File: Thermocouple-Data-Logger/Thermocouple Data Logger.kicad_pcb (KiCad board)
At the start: 4 copper layers, 75 x 85 mm, 149 parts, among them J0 Power, J1 Micro_SD_Card_Det, J2 Probe 1, J3 Probe 2, J4 Probe 3, J5 Probe 4, J6 ISP, SW0 Power, SW1 Display, SW2 Reset, SW3 Select/Calibrate, SW4 Cycle/Menu, SW5 SW_DIP_x04, U0 ATMEGA324PA-MU, U1 LT1763-3.3, U10 74HC595, U11 HDSP-521E-Display, U12 HDSP-521E-Display, U13 4050, U2 MAX31856, U3 MAX31856, U4 MAX31856, U5 MAX31856, U6 74HC595, U7 74HC595, U8 74HC595, U9 74HC595, Y0 10MHz, Y1 32.768KHz

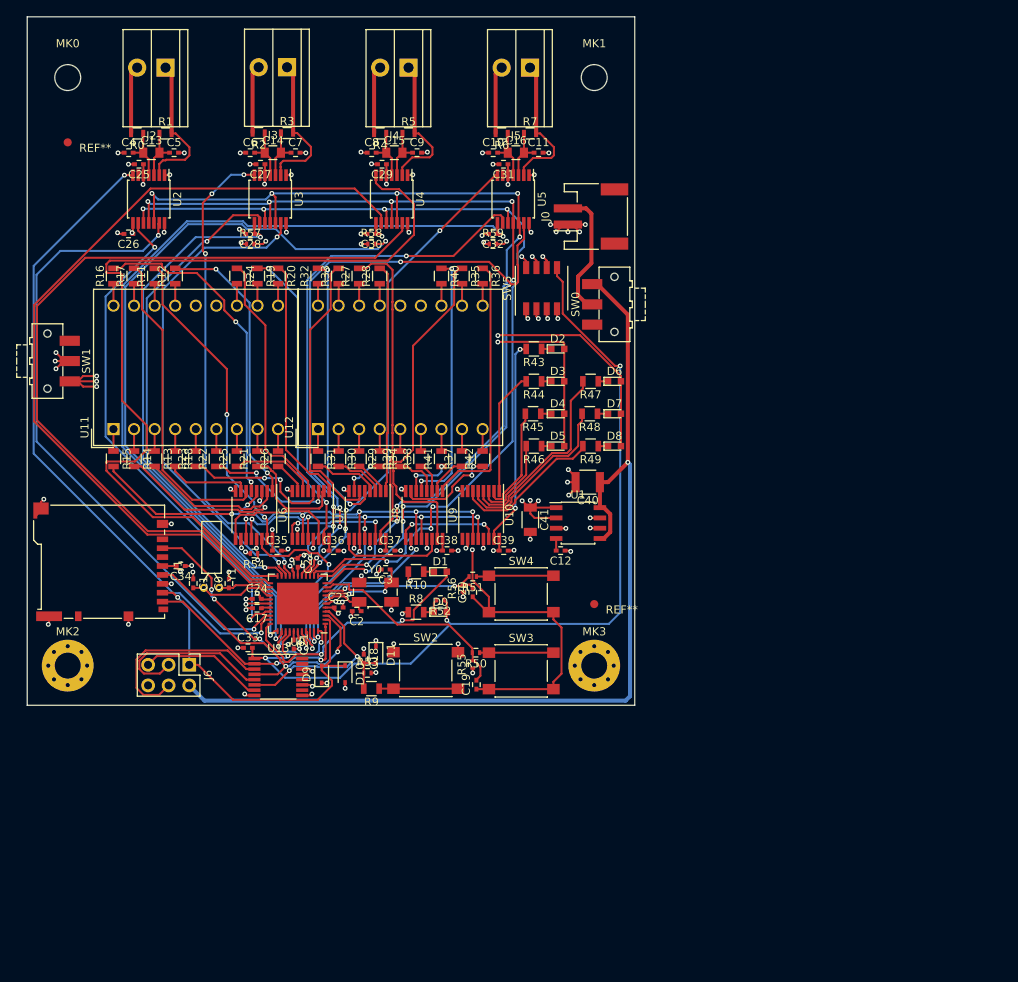
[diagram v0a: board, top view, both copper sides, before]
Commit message: Centerd board and generated gerber for test view
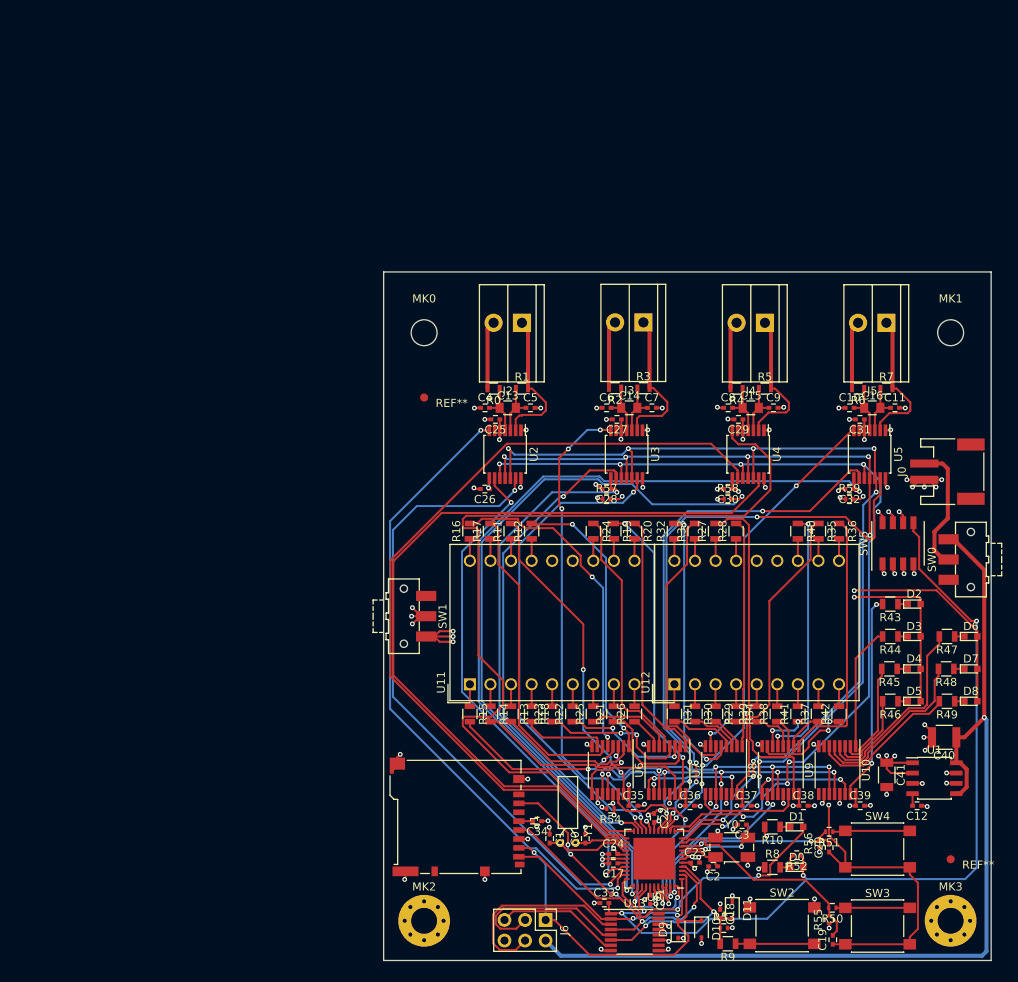
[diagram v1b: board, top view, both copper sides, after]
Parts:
- moved C17 54.1 mm to (137.4, 122.0)
- moved C18 54.1 mm to (150.6, 128.2)
- moved C2 54.1 mm to (149.7, 122.4)
- moved C27 54.1 mm to (137.8, 67.2)
- moved C29 54.1 mm to (152.8, 67.2)
- moved C31 54.1 mm to (167.8, 67.2)
- moved C41 54.1 mm to (171.1, 111.1)
- moved D11 54.1 mm to (152.1, 127.8)
- moved R43 54.1 mm to (171.6, 90.0)
- moved R44 54.1 mm to (171.6, 94.0)
- moved R46 54.1 mm to (171.6, 102.0)
- moved R56 54.1 mm to (162.8, 119.5)
- moved C0 54.1 mm to (133.9, 119.0)
- moved C1 54.1 mm to (129.5, 119.0)
- moved C10 54.1 mm to (166.5, 65.8)
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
